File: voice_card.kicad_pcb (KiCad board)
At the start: 2 copper layers, 119.3 x 38 mm, 207 parts, among them J1 PCI_11_49, Q1 MMBF4391LT1G, Q10 DMMT3906, Q11 BC857BS, Q2 2N3904, Q3 BCM847, Q4 DMMT3904, Q5 DMMT3906, Q6 MMBF4391LT1G, Q7 BCM847, Q8 2N3904, Q9 DMMT3904, U1 TL074-, U10 TL072-, U11 TL074-, U12 NE555, U13 LM311M, U14 CD4052, U15 TL072-, U16 TL072-, U17 LM13700, U18 LM13700, U19 LM13700, U2 TL074-, U20 TL072-, U3 NE555, U4 LF351, U5 TL072-, U6 LM311M, U7 CD4052, U8 TL074-, U9 LF351

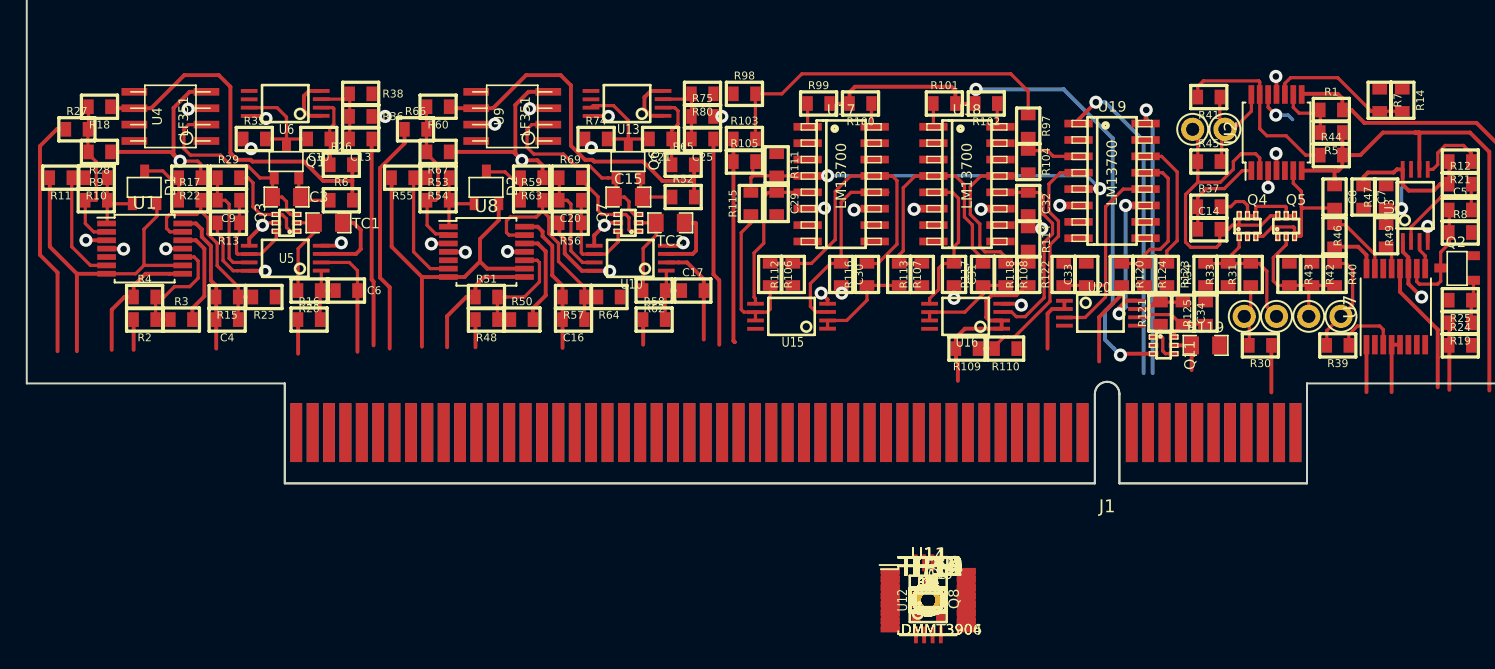
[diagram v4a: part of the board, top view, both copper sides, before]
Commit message: EG1 done, about to place EG2 components
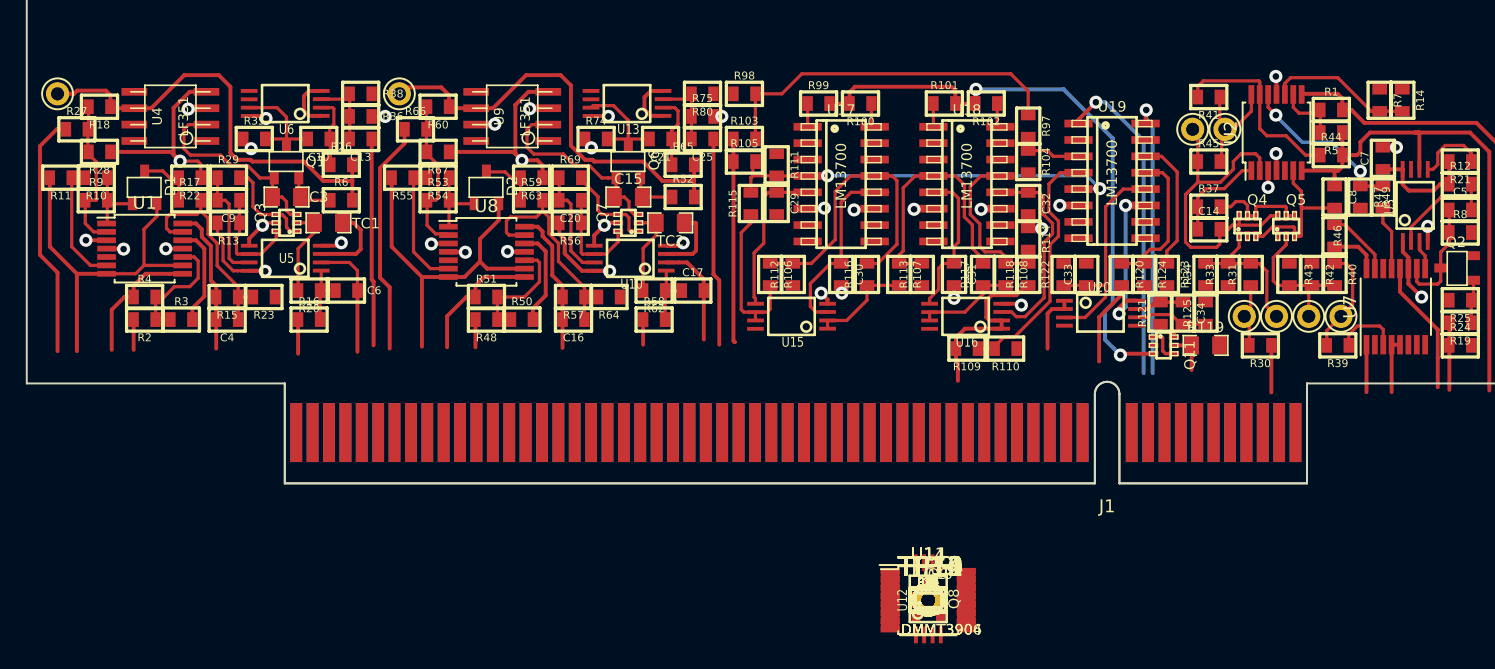
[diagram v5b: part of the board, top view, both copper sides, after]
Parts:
- moved TP1 78.1 mm to (81.0, 65.8)
- moved TP8 56.8 mm to (107.5, 65.8)
- moved C7 3.35 mm to (183.8, 70.8), turned to 90 degrees
- moved R49 3.01 mm to (183.8, 73.8)
- moved R47 2.00 mm to (182.0, 73.8), turned to 270 degrees
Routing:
- net Net-(R47-Pad1): track 7.53 -> 13.1 mm
- net Net-(R18-Pad1): track 29.1 -> 34.3 mm
- net Net-(R52-Pad2): track 29.4 -> 34.6 mm
- net Net-(R49-Pad1): track 1.88 -> 4.98 mm
- net +12V: track 54.5 -> 52.0 mm
- net GND: track 51.3 -> 52.4 mm, vias 13 -> 14

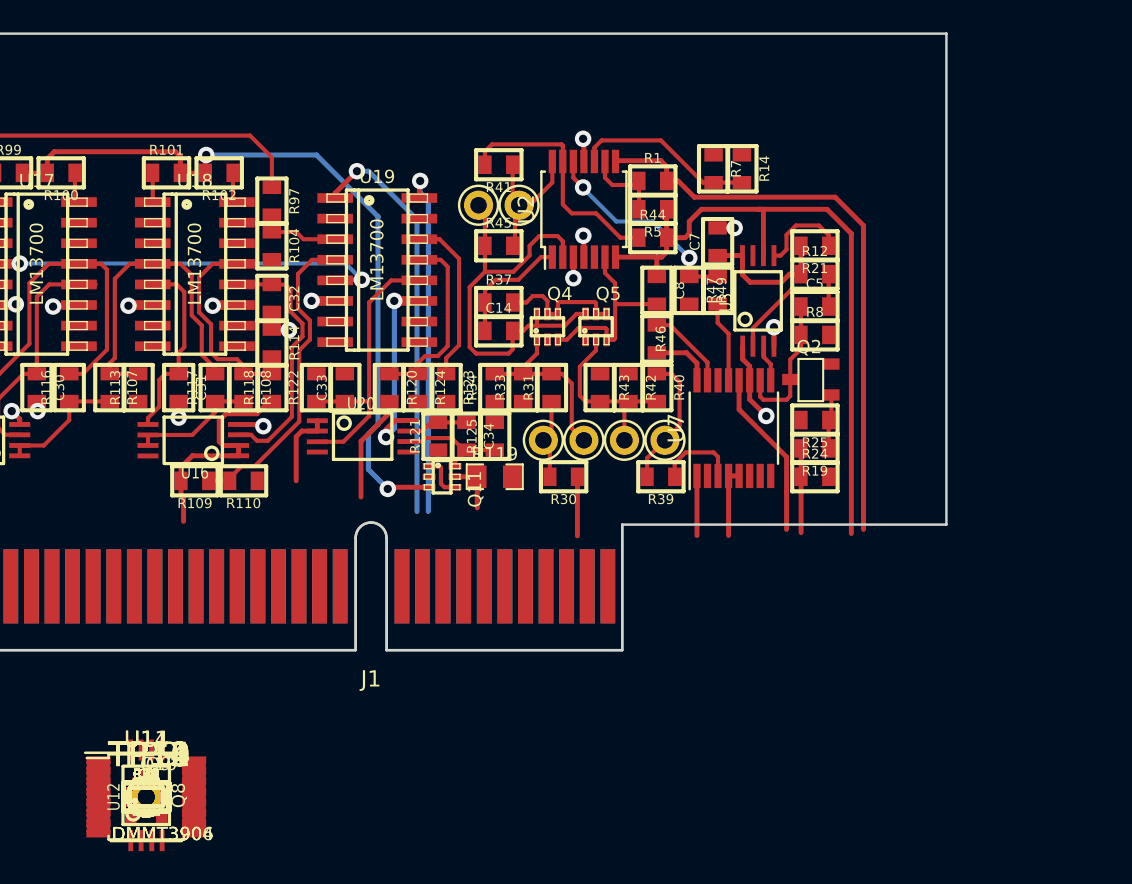
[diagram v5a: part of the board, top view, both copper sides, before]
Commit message: starting to place components for EG2
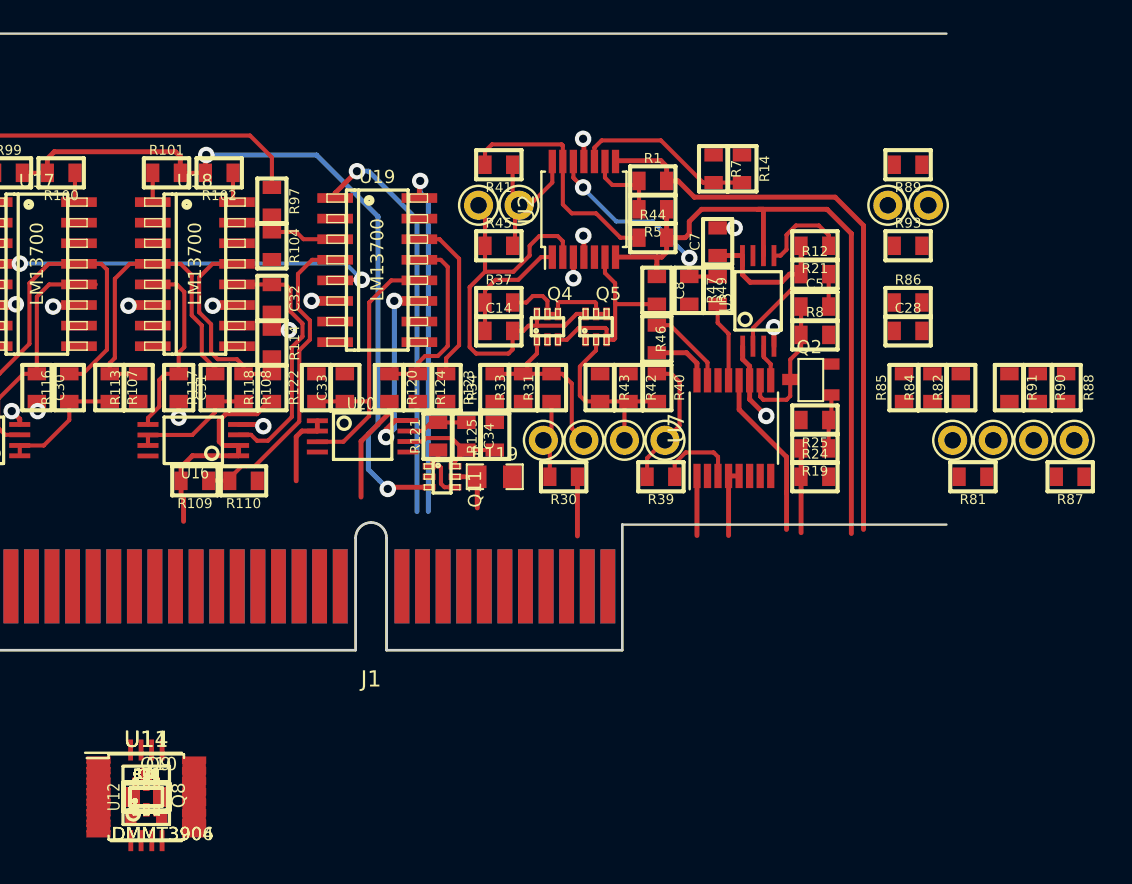
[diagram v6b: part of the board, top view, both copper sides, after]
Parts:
- moved R88 62.1 mm to (205.2, 79.8), turned to 270 degrees
- moved TP11 61.3 mm to (205.8, 83.0)
- moved R89 61.1 mm to (195.5, 66.0), turned to 180 degrees
- moved R90 60.5 mm to (203.5, 79.8), turned to 270 degrees
- moved TP14 60.5 mm to (196.8, 68.5)
- moved R87 60.3 mm to (205.5, 85.2), turned to 180 degrees
- moved TP12 59.0 mm to (203.2, 83.0)
- moved R91 58.9 mm to (201.8, 79.8), turned to 270 degrees
- moved TP13 58.5 mm to (194.2, 68.5)
- moved R93 58.0 mm to (195.5, 71.0)
- moved TP10 56.7 mm to (200.8, 83.0)
- moved R82 56.2 mm to (198.8, 79.8), turned to 90 degrees
- moved R86 56.0 mm to (195.5, 74.5)
- moved C28 55.1 mm to (195.5, 76.2)
- moved R81 54.7 mm to (199.5, 85.2), turned to 180 degrees
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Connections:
- U11 pad 1: EG2_INV_OUT -> Net-(C28-Pad1)
- U11 pad 10: GND -> Net-(R70-Pad2)
- U11 pad 2: Net-(R61-Pad1) -> Net-(C28-Pad2)
- U11 pad 3: Net-(R70-Pad2) -> GND
- U11 pad 8: Net-(C28-Pad1) -> EG2_INV_OUT
- U11 pad 9: Net-(C28-Pad2) -> Net-(R61-Pad1)

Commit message: EG2 placed and routed
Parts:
- moved R77 65.3 mm to (204.2, 71.0), turned to 180 degrees
- moved R72 64.4 mm to (204.2, 72.8)
- moved R73 64.3 mm to (199.8, 66.2), turned to 270 degrees
- moved C22 63.4 mm to (204.2, 74.8)
- moved R70 62.9 mm to (198.0, 66.2), turned to 270 degrees
- moved R71 62.6 mm to (204.2, 76.5)
- moved Q8 61.2 mm to (204.0, 79.2), turned to 90 degrees
- moved U12 60.5 mm to (200.8, 74.5)
- moved R79 60.4 mm to (204.2, 81.8), turned to 180 degrees
- moved C26 60.4 mm to (198.2, 70.8), turned to 90 degrees
- moved R76 59.8 mm to (204.2, 83.5), turned to 180 degrees
- moved R61 59.5 mm to (194.2, 67.0)
- moved R78 59.1 mm to (204.2, 85.2)
- moved R96 58.8 mm to (198.2, 73.8), turned to 90 degrees
- moved R68 58.4 mm to (194.2, 68.8), turned to 180 degrees
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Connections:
- Q10 pad 1: Net-(Q10-Pad1) -> GND
- Q10 pad 2: GND -> Net-(Q10-Pad2)
- Q10 pad 3: Net-(C28-Pad2) -> Net-(C27-Pad2)
- Q10 pad 6: Net-(C27-Pad2) -> Net-(C28-Pad2)
- R88 pad 2: Net-(Q10-Pad1) -> Net-(Q10-Pad2)
- R90 pad 2: Net-(Q10-Pad1) -> Net-(Q10-Pad2)
- R91 pad 2: Net-(Q10-Pad1) -> Net-(Q10-Pad2)
- TP12 pad 1: Net-(Q10-Pad1) -> Net-(Q10-Pad2)
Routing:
- net EG2_ENV_OUT: track 0.00 -> 37.8 mm
- net EG2_INV_OUT: track 0.00 -> 35.5 mm
- net Net-(C28-Pad2): track 0.00 -> 25.7 mm
- net Net-(R89-Pad2): track 0.00 -> 15.1 mm
- net +12V: track 52.0 -> 66.8 mm, vias 15 -> 17
- net Net-(R95-Pad1): track 0.00 -> 13.1 mm, vias 0 -> 2
- net Net-(C27-Pad2): track 0.00 -> 12.2 mm
- net Net-(Q9-Pad1): track 0.00 -> 11.6 mm
- net Net-(Q10-Pad2): track 0.00 -> 11.4 mm
- net Net-(R70-Pad2): track 0.00 -> 10.1 mm
- net EG2_SUSTAIN_CV: track 0.00 -> 9.47 mm
- net Net-(R89-Pad1): track 0.00 -> 9.26 mm
- net Net-(C22-Pad1): track 0.00 -> 9.04 mm
- net Net-(C22-Pad2): track 0.00 -> 8.69 mm
- net Net-(Q10-Pad4): track 0.00 -> 8.28 mm
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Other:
- board size 119.3 x 38 mm -> 139.3 x 32.8 mm
